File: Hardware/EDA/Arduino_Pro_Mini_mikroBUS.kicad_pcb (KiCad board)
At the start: 4 copper layers, 45.7 x 69.8 mm, 34 parts, among them J1 HEADER_F_2.54MM_1R8P_ST_AU_PTH, J2 HEADER_F_2.54MM_1R8P_ST_AU_PTH, J3 HEADER_F_2.54MM_1R12P_ST_AU_P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, J4 HEADER_F_2.54MM_1R12P_ST_AU_P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, J5 Molex_0475710001, J6 HEADER_F_2.54MM_1R2P_ST_AU_PTH, M1 FID, M2 FID, M3 FID, P1 HEADER_M_2.54MM_1R3P_ST_AU_PTH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

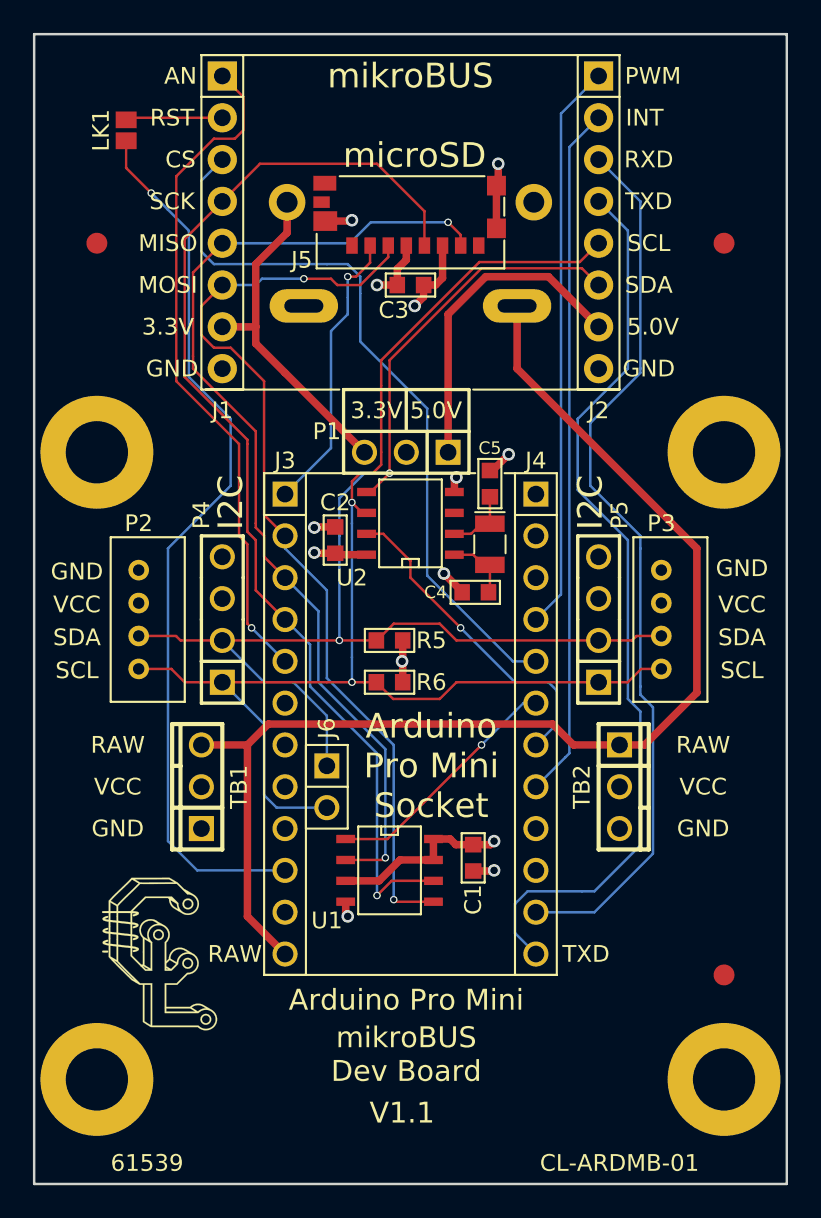
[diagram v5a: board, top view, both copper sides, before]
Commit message: Added layout for RTC crystal and caps. Re-routed several traces as-needed. Updated RTC and crystal component parameters in schematic and regenerated netlist. Gerbers generated - need final review before release.
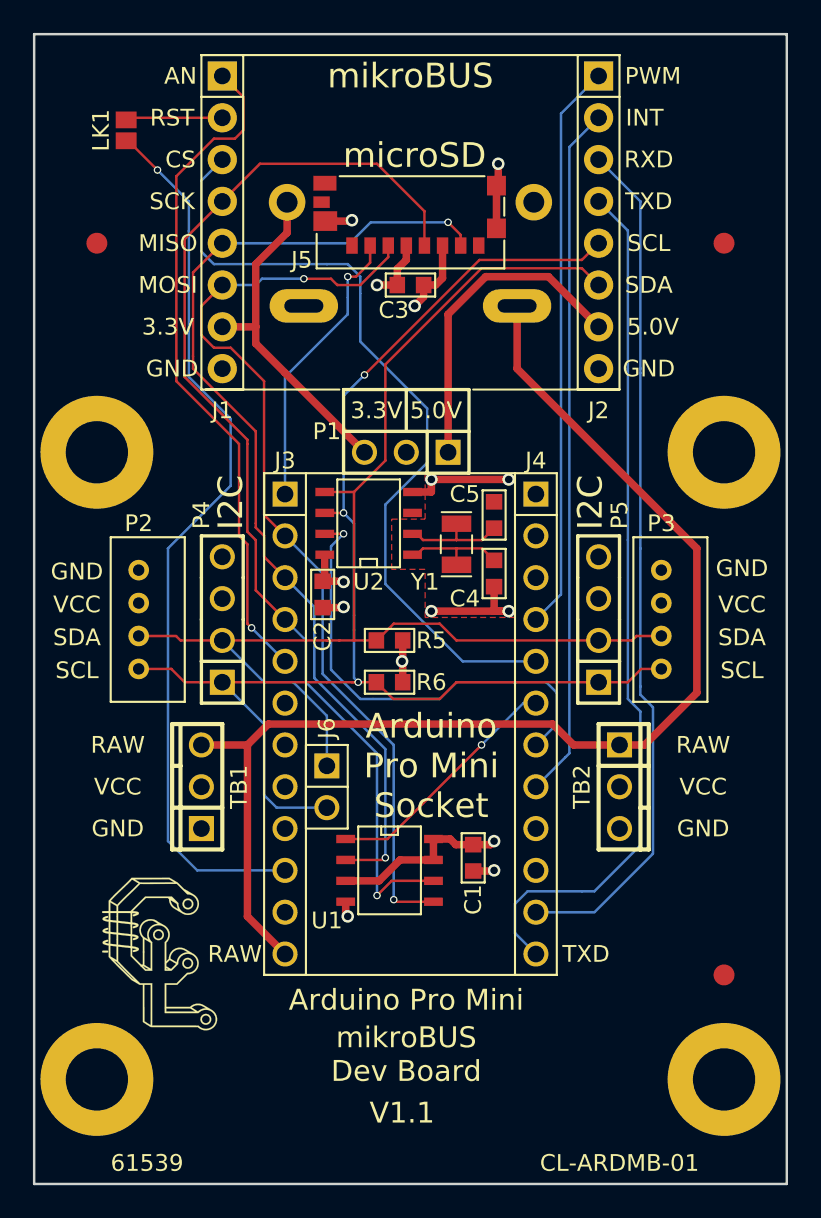
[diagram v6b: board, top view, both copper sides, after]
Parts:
- C4, C5: value 12pF -> 6pF
- U1: value FL127 -> FL116K
- Y1: footprint Crystals:Crystal_SMD_G8-2pin_3.2x1.5mm -> Passive:XTAL_3.2MM_1.5MM_SMT_ALT
- moved C2 3.39 mm to (74.7, 65.8), turned to 270 degrees
- moved U2 2.54 mm to (77.5, 61.5)
- moved Y1 2.03 mm to (82.8, 62.7)
- moved C5 1.92 mm to (85.1, 61.0)
- moved C4 1.62 mm to (85.1, 64.5), turned to 270 degrees
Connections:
- net mikroBUS_RST renamed /mikroBUS_RST
- J3 pad 6: A1 -> (no net)
- J3 pad 7: A2 -> (no net)
- J3 pad 8: A3 -> (no net)
- J4 pad 1: D9 -> (no net)
- J4 pad 10: RST -> (no net)
- J4 pad 2: D8 -> (no net)
- J4 pad 3: D7 -> (no net)
- J5 pad 1: Net-(J5-Pad1) -> (no net)
- J5 pad 12: Net-(J5-Pad12) -> (no net)
- J5 pad 13: Net-(J5-Pad13) -> (no net)
- J5 pad 8: Net-(J5-Pad8) -> (no net)
- M1 pad ~: Net-(M1-Pad~) -> (no net)
- M2 pad ~: Net-(M2-Pad~) -> (no net)
- M3 pad ~: Net-(M3-Pad~) -> (no net)
- U2 pad 3: Net-(U2-Pad3) -> (no net)
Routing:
- net GND: track 18.0 -> 27.6 mm, vias 9 -> 10
- net D3: track 19.9 -> 28.9 mm
- net D5: track 45.0 -> 48.9 mm
- net TXD: track 55.4 -> 52.8 mm
- net RXD: track 54.6 -> 52.1 mm
- net Net-(C5-Pad1): track 4.05 -> 6.41 mm
- net Net-(C4-Pad1): track 4.38 -> 6.41 mm
- net SDA: track 80.6 -> 79.2 mm, vias 2 -> 0
- net SCL: track 83.3 -> 83.5 mm, vias 2 -> 3
- added copper zone on F.Cu, net GND
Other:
- board text added: "Corrections made: Added crystal, caps and ground pour for RTC Corrected pin numbering of 2xAA battery holder footprint to match schematic decal Corrected pin numbering of 1x9V battery holder footprint to match schematic decal Re-layed out 2xAA battery traces Re-layed out 1x9V battery traces Added silkscreen pin names to Grove connector Add silkscreen orientation to Arduino socket Add silkscreen p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"
- board text added: "Corrections needed:"
- board text removed: "Corrections made: Corrected pin numbering of 2xAA battery holder footprint to match schematic decal Corrected pin numbering of 1x9V battery holder footprint to match schematic decal Re-layed out 2xAA battery traces Re-layed out 1x9V battery traces Added silkscreen pin names to Grove connector Add silkscreen orientation to Arduino socket Add silkscreen pin names to mikroBUS connector"
- board text removed: "Corrections needed: RTC needs crystal and caps Check FL127 footprint against Winbond footprint Add level shifter for microSD socket?"

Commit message: Updated date in schematic and PCB title block. Regenerated PDF schematic. Verified gerbers.
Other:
- board text removed: "Corrections made: Added crystal, caps and ground pour for RTC Corrected pin numbering of 2xAA battery holder footprint to match schematic decal Corrected pin numbering of 1x9V battery holder footprint to match schematic decal Re-layed out 2xAA battery traces Re-layed out 1x9V battery traces Added silkscreen pin names to Grove connector Add silkscreen orientation to Arduino socket Add silkscreen p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"
- board text removed: "Corrections needed:"
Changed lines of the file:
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@@
     (links 87)
     (no_connects 0)
-    (area 41.374287 21.6 218.229426 113.190001)
+    (area 41.374287 23.97 117.375715 113.190001)
     (thickness 1.6)
-    (drawings 66)
+    (drawings 64)
     (tracks 322)
     (zones 0)
@@
   (title_block
     (title "Arduino Pro Mini mikroBUS Develepment Board")
-    (date 2018-02-11)
+    (date 2018-04-07)
     (rev 1.1)
     (company "Casco Logix, LLC")
@@
     (effects (font (size 1.016 1.016) (thickness 0.2032)))
   )
-  (gr_text "Corrections needed:\n" (at 121.15 22.8) (layer Cmts.User)
-    (effects (font (size 1.5 1.5) (thickness 0.3)) (justify left))
-  )
-  (gr_text "Corrections made:\nAdded crystal, caps and ground pour for RTC\nCorrected pin numbering of 2xAA battery holder footprint to match schematic decal\nCorrected pin numbering of 1x9V battery holder footprint to match schematic decal\nRe-layed out 2xAA battery traces\nRe-layed out 1x9V battery traces\nAdded silkscreen pin names to Grove connector\nAdd silkscreen orientation to Arduino socket\nAdd silkscreen pin names to mikroBUS connector\nVerified flash functionality through testing" (at 121.158 43.18) (layer Cmts.User)
-    (effects (font (size 1.5 1.5) (thickness 0.3)) (justify left))
-  )
   (dimension 41.91 (width 0.3) (layer Dwgs.User)
